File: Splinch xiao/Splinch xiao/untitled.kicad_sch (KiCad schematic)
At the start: 68 parts, among them SW1 Switch, U2 Seeeduino Xiao nRF52840

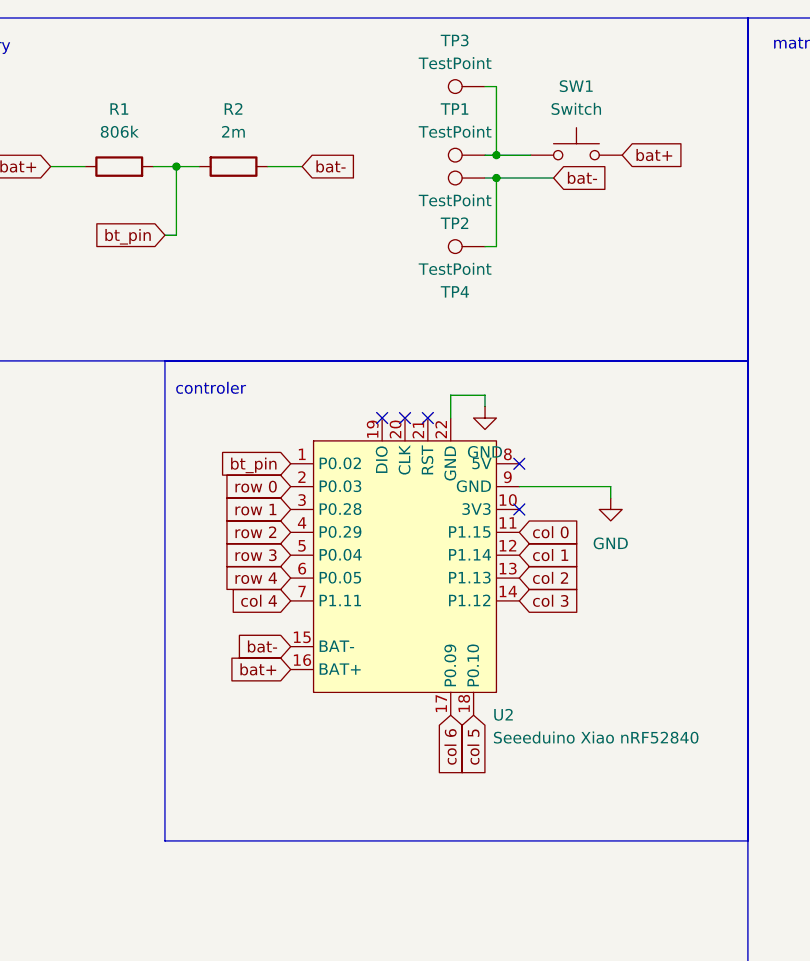
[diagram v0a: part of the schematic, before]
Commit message: case' wiring and more
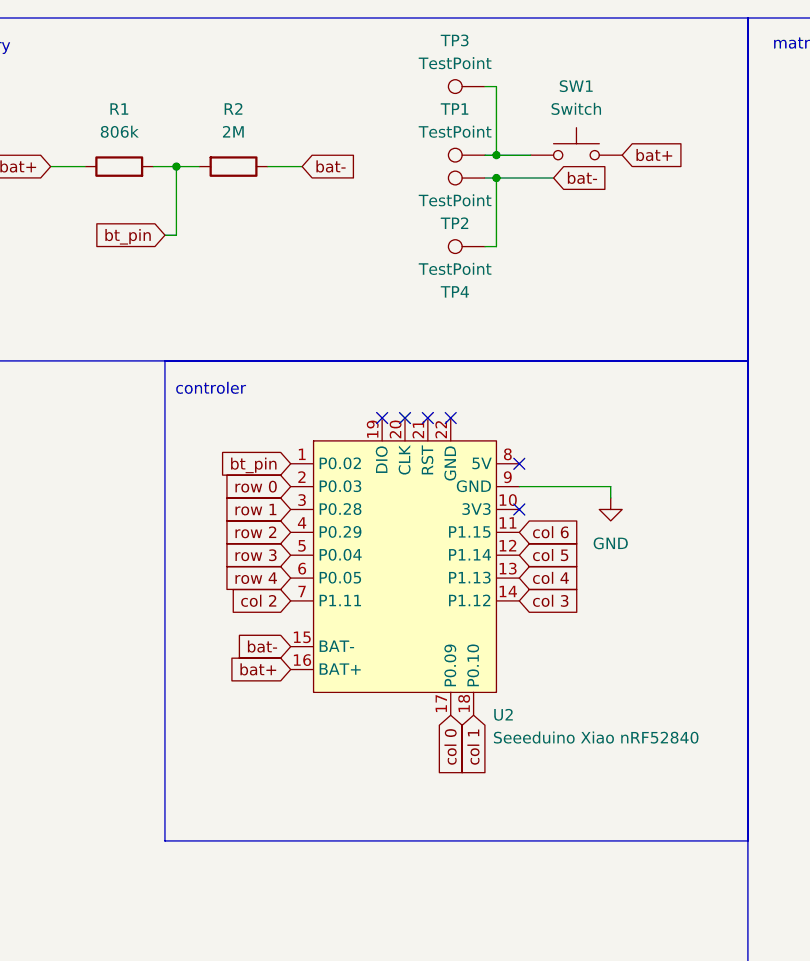
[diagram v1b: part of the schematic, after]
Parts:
- R2: value 2m -> 2M
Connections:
- net GND: no longer U2.22 (GND)
- net col 0: now also U2.17 (P0.09); no longer U2.11 (P1.15)
- net col 1: now also U2.18 (P0.10); no longer U2.12 (P1.14)
- net col 2: now also U2.7 (P1.11); no longer U2.13 (P1.13)
- net col 4: now also U2.13 (P1.13); no longer U2.7 (P1.11)
- net col 5: now also U2.12 (P1.14); no longer U2.18 (P0.10)
- net col 6: now also U2.11 (P1.15); no longer U2.17 (P0.09)
- no-connect marks 5 -> 6
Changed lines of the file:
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@@
 	)
 	(no_connect
+		(at 114.3 46.99)
+	)
+	(no_connect
 		(at 111.76 46.99)
 	)
@@
 	(wire
 		(pts
-			(xy 114.3 46.99) (xy 114.3 44.45)
-		)
-		(stroke
-			(width 0)
-			(type default)
-		)
-	)
-	(wire
-		(pts
 			(xy 118.11 10.16) (xy 119.38 10.16)
 		)
@@
 	(wire
 		(pts
-			(xy 114.3 44.45) (xy 118.11 44.45)
-		)
-		(stroke
-			(width 0)
-			(type default)
-		)
-	)
-	(wire
-		(pts
 			(xy 227.33 24.13) (xy 227.33 34.29)
 		)
@@
 	(wire
 		(pts
-			(xy 118.11 44.45) (xy 118.11 45.72)
-		)
-		(stroke
-			(width 0)
-			(type default)
-		)
-	)
-	(wire
-		(pts
 			(xy 217.17 80.01) (xy 217.17 93.98)
 		)
@@
 		)
 	)
+	(global_label "col 2"
+		(shape input)
+		(at 96.52 67.31 180)
+		(fields_autoplaced yes)
+		(effects
+			(font
+				(size 1.27 1.27)
+			)
+			(justify right)
+		)
+		(property "Intersheetrefs" "${INTERSHEET_REFS}"
+			(at 88.4549 67.31 0)
+			(effects
+				(font
+					(size 1.27 1.27)
+				)
+				(justify right)
+				(hide yes)
+			)
+		)
+	)
 	(global_label "col 3"
 		(shape input)
@@
 		)
 	)
-	(global_label "col 5"
+	(global_label "bat+"
 		(shape input)
-		(at 116.84 80.01 270)
+		(at 133.35 17.78 0)
 		(fields_autoplaced yes)
 		(effects
@@
 				(size 1.27 1.27)
 			)
-			(justify right)
+			(justify left)
 		)
 		(property "Intersheetrefs" "${INTERSHEET_REFS}"
-			(at 116.84 88.0751 90)
+			(at 140.9313 17.78 0)
 			(effects
 				(font
 					(size 1.27 1.27)
 				)
-				(justify right)
+				(justify left)
 				(hide yes)
 			)
 		)
 	)
-	(global_label "bat+"
+	(global_label "bt_pin"
 		(shape input)
-		(at 133.35 17.78 0)
+		(at 82.55 26.67 180)
 		(fields_autoplaced yes)
 		(effects
@@
 				(size 1.27 1.27)
 			)
-			(justify left)
+			(justify right)
 		)
 		(property "Intersheetrefs" "${INTERSHEET_REFS}"
-			(at 140.9313 17.78 0)
+			(at 73.8197 26.67 0)
 			(effects
 				(font
 					(size 1.27 1.27)
 				)
-				(justify left)
+				(justify right)
 				(hide yes)
 			)
 		)
 	)
-	(global_label "bt_pin"
+	(global_label "col 3"
 		(shape input)
-		(at 82.55 26.67 180)
+		(at 121.92 67.31 0)
 		(fields_autoplaced yes)
 		(effects
@@
 				(size 1.27 1.27)
 			)
-			(justify right)
+			(justify left)
 		)
 		(property "Intersheetrefs" "${INTERSHEET_REFS}"
-			(at 73.8197 26.67 0)
+			(at 129.9851 67.31 0)
 			(effects
 				(font
 					(size 1.27 1.27)
 				)
-				(justify right)
+				(justify left)
 				(hide yes)
 			)
@@
 		)
 	)
-	(global_label "col 4"
-		(shape input)
-		(at 96.52 67.31 180)
-		(fields_autoplaced yes)
-		(effects
-			(font
-				(size 1.27 1.27)
-			)
-			(justify right)
-		)
-		(property "Intersheetrefs" "${INTERSHEET_REFS}"
-			(at 88.4549 67.31 0)
-			(effects
-				(font
-					(size 1.27 1.27)
-				)
-				(justify right)
-				(hide yes)
-			)
-		)
-	)
 	(global_label "row 3"
 		(shape input)
@@
 		)
 	)
-	(global_label "col 3"
+	(global_label "col 6"
 		(shape input)
-		(at 121.92 67.31 0)
+		(at 248.92 24.13 90)
 		(fields_autoplaced yes)
 		(effects
@@
 		)
 		(property "Intersheetrefs" "${INTERSHEET_REFS}"
-			(at 129.9851 67.31 0)
+			(at 248.92 16.0649 90)
 			(effects
 				(font
@@
 		)
 	)
-	(global_label "col 6"
+	(global_label "col 4"
 		(shape input)
-		(at 248.92 24.13 90)
+		(at 227.33 24.13 90)
 		(fields_autoplaced yes)
 		(effects
@@
 		)
 		(property "Intersheetrefs" "${INTERSHEET_REFS}"
-			(at 248.92 16.0649 90)
+			(at 227.33 16.0649 90)
 			(effects
 				(font
@@
 		)
 	)
-	(global_label "col 0"
+	(global_label "col 5"
 		(shape input)
-		(at 121.92 59.69 0)
+		(at 237.49 24.13 90)
 		(fields_autoplaced yes)
 		(effects
@@
 		)
 		(property "Intersheetrefs" "${INTERSHEET_REFS}"
-			(at 129.9851 59.69 0)
+			(at 237.49 16.0649 90)
 			(effects
 				(font
@@
 		)
 	)
-	(global_label "col 4"
+	(global_label "row 4"
 		(shape input)
-		(at 227.33 24.13 90)
+		(at 96.52 64.77 180)
 		(fields_autoplaced yes)
 		(effects
@@
 				(size 1.27 1.27)
 			)
-			(justify left)
+			(justify right)
 		)
 		(property "Intersheetrefs" "${INTERSHEET_REFS}"
-			(at 227.33 16.0649 90)
+			(at 88.092 64.77 0)
 			(effects
 				(font
 					(size 1.27 1.27)
 				)
-				(justify left)
+				(justify right)
 				(hide yes)
 			)
 		)
 	)
-	(global_label "col 1"
+	(global_label "col 4"
 		(shape input)
-		(at 121.92 62.23 0)
+		(at 121.92 64.77 0)
 		(fields_autoplaced yes)
 		(effects
@@
 		)
 		(property "Intersheetrefs" "${INTERSHEET_REFS}"
-			(at 129.9851 62.23 0)
+			(at 129.9851 64.77 0)
 			(effects
 				(font
@@
 		)
 	)
-	(global_label "col 5"
+	(global_label "col 6"
 		(shape input)
-		(at 237.49 24.13 90)
+		(at 121.92 59.69 0)
 		(fields_autoplaced yes)
 		(effects
@@
 		)
 		(property "Intersheetrefs" "${INTERSHEET_REFS}"
-			(at 237.49 16.0649 90)
+			(at 129.9851 59.69 0)
 			(effects
 				(font
@@
 		)
 	)
-	(global_label "row 4"
+	(global_label "col 1"
 		(shape input)
-		(at 96.52 64.77 180)
+		(at 116.84 80.01 270)
 		(fields_autoplaced yes)
 		(effects
@@
 		)
 		(property "Intersheetrefs" "${INTERSHEET_REFS}"
-			(at 88.092 64.77 0)
+			(at 116.84 88.0751 90)
 			(effects
 				(font
@@
 		)
 	)
-	(global_label "col 2"
+	(global_label "col 0"
 		(shape input)
-		(at 121.92 64.77 0)
+		(at 114.3 80.01 270)
 		(fields_autoplaced yes)
 		(effects
@@
 				(size 1.27 1.27)
 			)
-			(justify left)
+			(justify right)
 		)
 		(property "Intersheetrefs" "${INTERSHEET_REFS}"
-			(at 129.9851 64.77 0)
+			(at 114.3 88.0751 90)
 			(effects
 				(font
 					(size 1.27 1.27)
 				)
-				(justify left)
+				(justify right)
 				(hide yes)
 			)
 		)
 	)
-	(global_label "col 6"
+	(global_label "row 2"
 		(shape input)
-		(at 114.3 80.01 270)
+		(at 162.56 77.47 180)
 		(fields_autoplaced yes)
 		(effects
@@
 		)
 		(property "Intersheetrefs" "${INTERSHEET_REFS}"
-			(at 114.3 88.0751 90)
+			(at 154.132 77.47 0)
 			(effects
 				(font
@@
 	(global_label "row 2"
 		(shape input)
-		(at 162.56 77.47 180)
+		(at 96.52 59.69 180)
 		(fields_autoplaced yes)
 		(effects
@@
 		)
 		(property "Intersheetrefs" "${INTERSHEET_REFS}"
-			(at 154.132 77.47 0)
+			(at 88.092 59.69 0)
 			(effects
 				(font
@@
 		)
 	)
-	(global_label "row 2"
+	(global_label "col 5"
 		(shape input)
-		(at 96.52 59.69 180)
+		(at 121.92 62.23 0)
 		(fields_autoplaced yes)
 		(effects
@@
 				(size 1.27 1.27)
 			)
-			(justify right)
+			(justify left)
 		)
 		(property "Intersheetrefs" "${INTERSHEET_REFS}"
-			(at 88.092 59.69 0)
+			(at 129.9851 62.23 0)
 			(effects
 				(font
 					(size 1.27 1.27)
 				)
-				(justify right)
+				(justify left)
 				(hide yes)
 			)
@@
 	)
 	(symbol
-		(lib_id "power:GND")
-		(at 118.11 45.72 0)
-		(unit 1)
-		(exclude_from_sim no)
-		(in_bom yes)
-		(on_board yes)
-		(dnp no)
-		(fields_autoplaced yes)
-		(property "Reference" "#PWR02"
-			(at 118.11 52.07 0)
-			(effects
-				(font
-					(size 1.27 1.27)
-				)
-				(hide yes)
-			)
-		)
-		(property "Value" "GND"
-			(at 118.11 50.8 0)
-			(effects
-				(font
-					(size 1.27 1.27)
-				)
-			)
-		)
-		(property "Footprint" ""
-			(at 118.11 45.72 0)
-			(effects
-				(font
-					(size 1.27 1.27)
-				)
-				(hide yes)
-			)
-		)
-		(property "Datasheet" ""
-			(at 118.11 45.72 0)
-			(effects
-				(font
-					(size 1.27 1.27)
-				)
-				(hide yes)
-			)
-		)
-		(property "Description" "Power symbol creates a global label with name \"GND\" , ground"
-			(at 118.11 45.72 0)
-			(effects
-				(font
-					(size 1.27 1.27)
-				)
-				(hide yes)
-			)
-		)
-		(pin "1"
-		)
-		(instances
-			(project "Splinch xiao"
-				(path "/c515e41c-2fc4-46fc-9db0-652f4126e058/1122df47-423a-4c05-9f09-3250746da53b"
-					(reference "#PWR02")
-					(unit 1)
-				)
-			)
-		)
-	)
-	(symbol
 		(lib_id "ScottoKeebs:Placeholder_Diode")
 		(at 198.12 102.87 90)
@@
 			)
 		)
-		(property "Value" "2m"
+		(property "Value" "2M"
 			(at 90.17 15.24 90)
 			(effects

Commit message: added silk screen and reade me
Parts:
- D1, D10, D11, D12, D13, D14, D15, D16, D17, D18, D19, D2, D20, D21, D22, D23, D24, D25, D26, D27, D28, D29, D3, D30, D35'1, D4, D5, D7, D8, D9: LCSC (none) -> C2128
- R1: LCSC (none) -> C121025
- R2: LCSC (none) -> C106170
